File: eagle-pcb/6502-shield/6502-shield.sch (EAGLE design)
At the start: 28 parts, among them CON1 M20-7821646-FEM-HDR, SW1 MCSLPT4644B1TR-TACT-SW, SW2 PCM12SMTR-SPDT-RIGHT-ANG, U1 AT28C256TSOP-28, U13 74HC32TSSOP-14, U17 74HC04TSSOP-14, U2 W65C02S, U3 AS6C62256, U4 W65C22, U5 MM74HC00TSSOP, U6 SE555QS, U7 SE555QS, U8 SE555QS

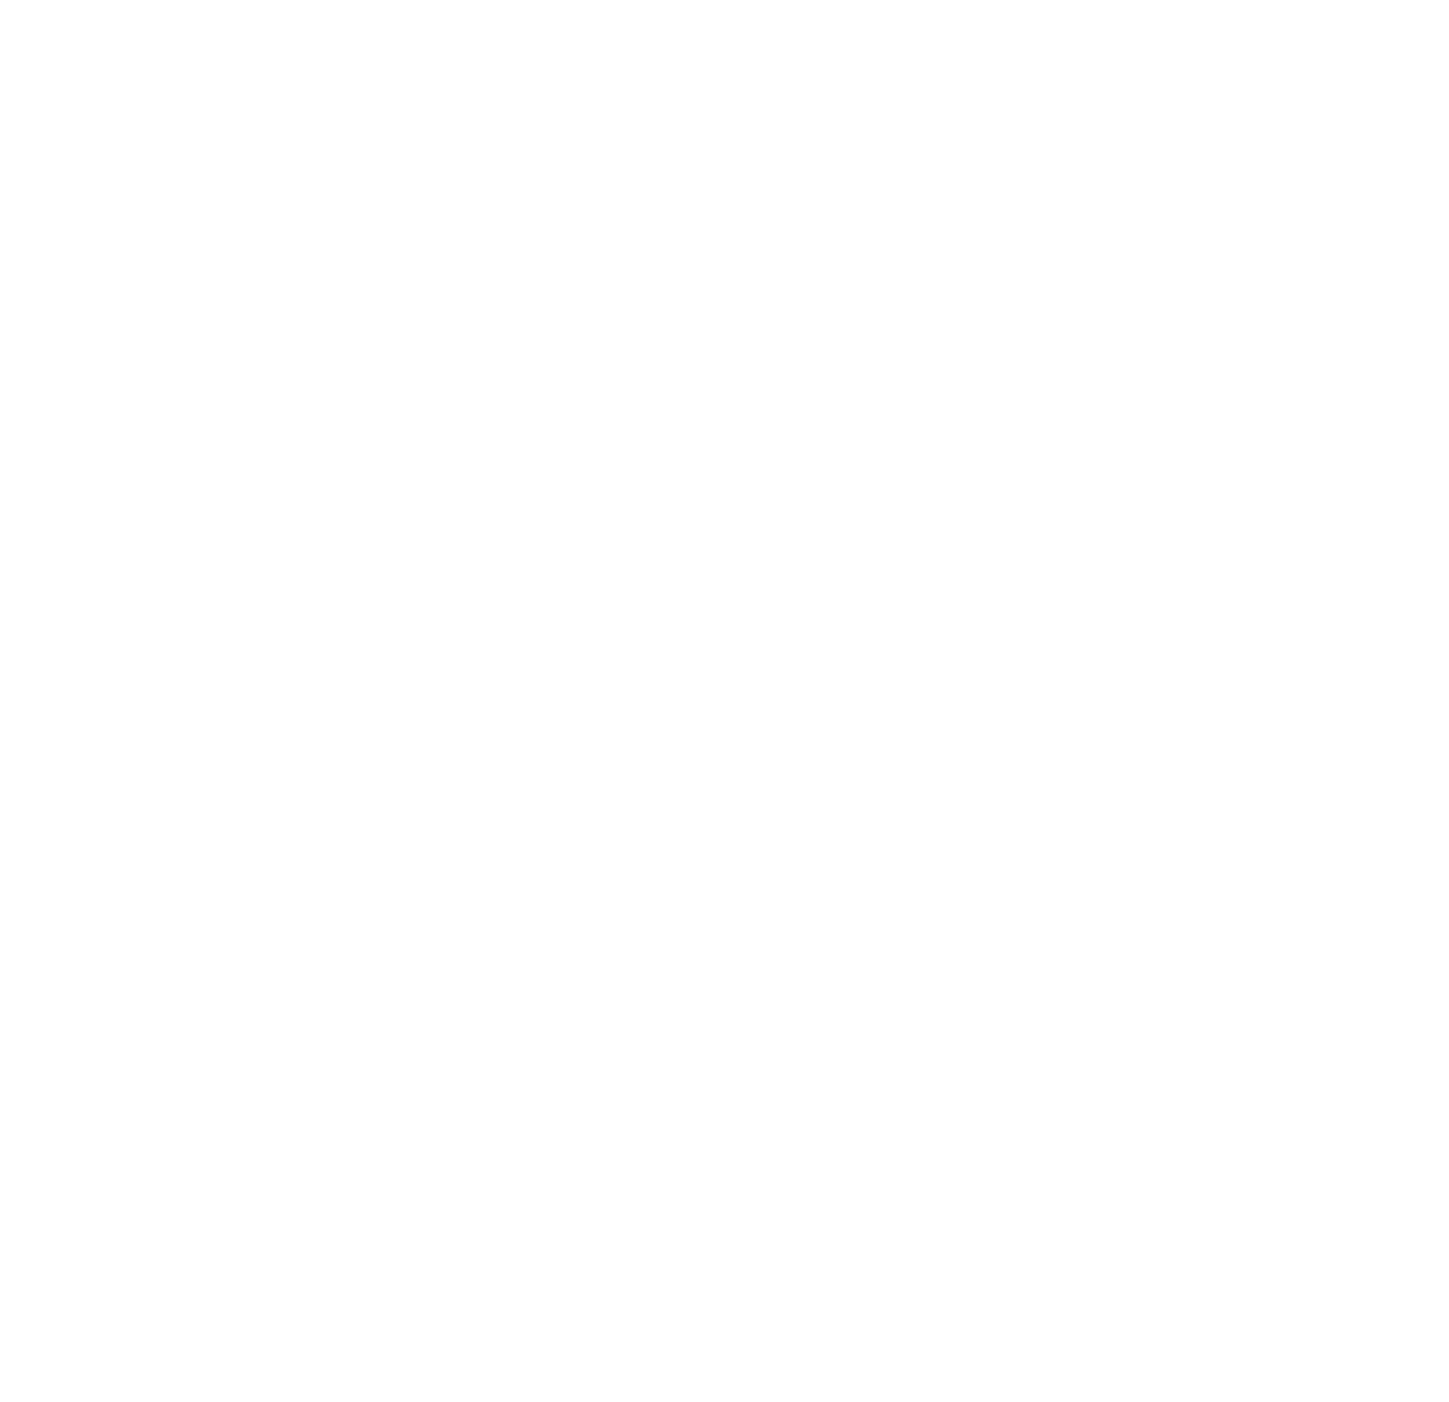
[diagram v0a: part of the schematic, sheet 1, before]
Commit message: added lattice machx02-256 FPGA in tqfp100 package - symbol, footprint, 3d model
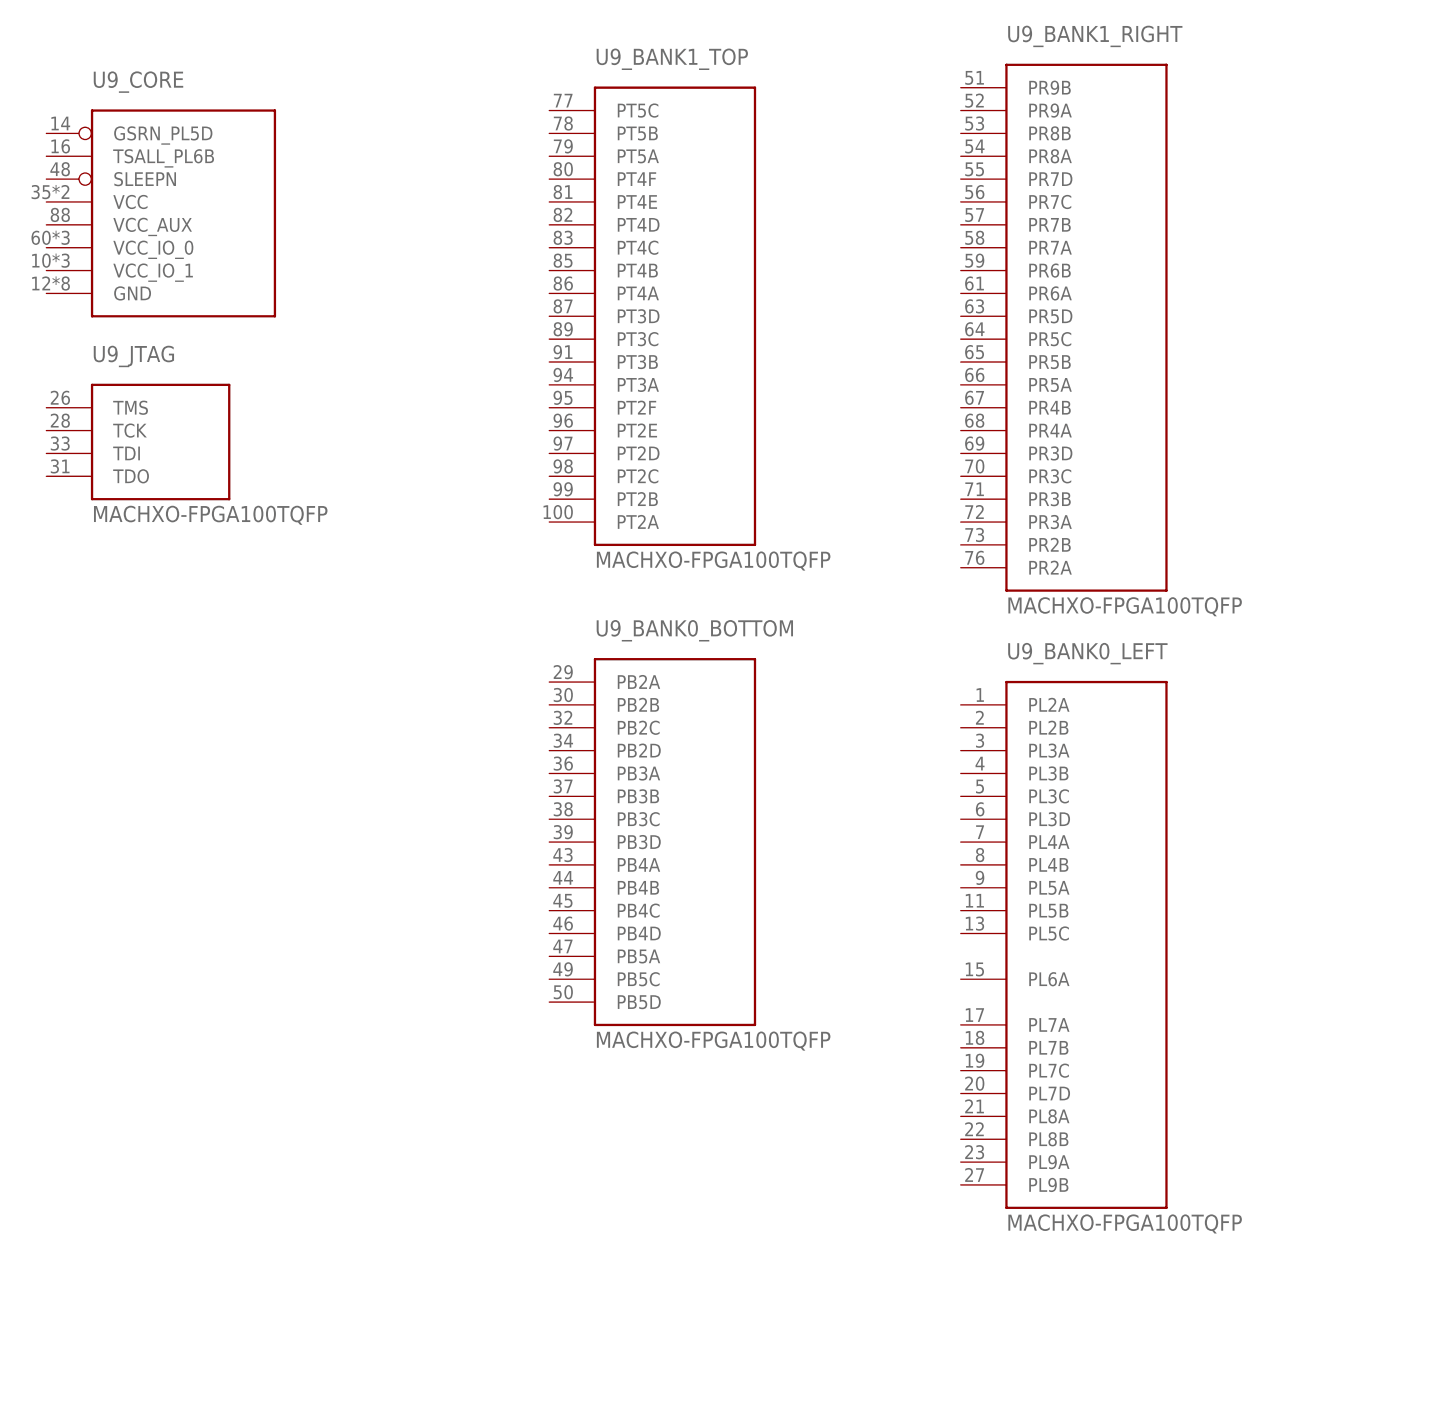
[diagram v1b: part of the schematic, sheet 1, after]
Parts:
- added U9: MACHXO-FPGA100TQFP, 6502-shield:MACHXO-FPGA100TQFP
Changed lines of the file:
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@@
 <setting verticaltext="up"/>
 </settings>
-<grid distance="0.01" unitdist="inch" unit="inch" style="lines" multiple="1" display="yes" altdistance="0.001" altunitdist="inch" altunit="inch"/>
+<grid distance="0.1" unitdist="inch" unit="inch" style="lines" multiple="1" display="no" altdistance="0.01" altunitdist="inch" altunit="inch"/>
 <layers>
 <layer number="1" name="Top" color="4" fill="1" visible="no" active="no"/>
@@
 <part name="GND22" library="supply1" library_urn="urn:adsk.eagle:library:371" deviceset="GND" device=""/>
 <part name="CON1" library="6502-shield" library_urn="urn:adsk.eagle:library:18477216" deviceset="M20-7821646-FEM-HDR" device="" package3d_urn="urn:adsk.eagle:package:18698632/1"/>
+<part name="U9" library="6502-shield" library_urn="urn:adsk.eagle:library:18477216" deviceset="MACHXO-FPGA" device="100TQFP" package3d_urn="urn:adsk.eagle:package:18828921/1"/>
 </parts>
 <sheets>
@@
 <attribute name="VALUE" x="195.58" y="37.846" size="1.27" layer="96"/>
 </instance>
+<instance part="U9" gate="_JTAG" x="-246.38" y="170.18" smashed="yes">
+<attribute name="NAME" x="-254" y="177.8" size="1.778" layer="95"/>
+<attribute name="VALUE" x="-254" y="160.02" size="1.778" layer="96"/>
+</instance>
+<instance part="U9" gate="_CORE" x="-243.84" y="195.58" smashed="yes">
+<attribute name="NAME" x="-254" y="208.28" size="1.778" layer="95"/>
+</instance>
+<instance part="U9" gate="_BANK1_TOP" x="-187.96" y="182.88" smashed="yes">
+<attribute name="NAME" x="-198.12" y="210.82" size="1.778" layer="95"/>
+<attribute name="VALUE" x="-198.12" y="154.94" size="1.778" layer="96"/>
+</instance>
+<instance part="U9" gate="_BANK1_RIGHT" x="-142.24" y="182.88" smashed="yes">
+<attribute name="NAME" x="-152.4" y="213.36" size="1.778" layer="95"/>
+<attribute name="VALUE" x="-152.4" y="149.86" size="1.778" layer="96"/>
+</instance>
+<instance part="U9" gate="_BANK0_LEFT" x="-142.24" y="114.3" smashed="yes">
+<attribute name="NAME" x="-152.4" y="144.78" size="1.778" layer="95"/>
+<attribute name="VALUE" x="-152.4" y="81.28" size="1.778" layer="96"/>
+</instance>
+<instance part="U9" gate="_BANK0_BOTTOM" x="-187.96" y="124.46" smashed="yes">
+<attribute name="NAME" x="-198.12" y="147.32" size="1.778" layer="95"/>
+<attribute name="VALUE" x="-198.12" y="101.6" size="1.778" layer="96"/>
+</instance>
 </instances>

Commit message: got the fpga based design done (first pass).  Notional parts placement, no routing.
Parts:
- removed C1: 1uF, rcl:C-USC0805
- removed C2, C5, C7: 0.01uF, rcl:C-USC0402
- removed C6: 0.1uF, rcl:C-USC0402
- removed CON1: M20-7821646-FEM-HDR, 6502-shield:M20-7821646-FEM-HDR
- removed U13: 74HC32TSSOP-14, 6502-shield:74HC32TSSOP-14
- removed U17: 74HC04TSSOP-14, 6502-shield:74HC04TSSOP-14
- removed U6, U7, U8: SE555QS, 6502-shield:SE555QS
- removed U9: MACHXO-FPGA100TQFP, 6502-shield:MACHXO-FPGA100TQFP
- added D1, D2, D3, D4, D5, D6, D7: (no value), we-led:WL-SMCD_0603_150060SS55040
- added D10, D8, D9: ACDC02-41SGWA-DUAL-7SEG, 6502-shield:ACDC02-41SGWA-DUAL-7SEG
- added JP1: (no value), pinhead:PINHD-2X3
- added JP2: (no value), pinhead:PINHD-2X8
- added JP3: (no value), pinhead:PINHD-1X3
- added R10, R11, R12, R13, R14, R15, R16, R17: 330, rcl:R-US_R0402
- added R18: 10K, rcl:R-US_R0402
- added R19: 10K, 6502-shield:TRIMPOTTC33X
- added R8, R9: 390, rcl:R-US_R0402
- added SJ1: (no value), jumper:SJ2W
- added SW3: MCSLPT4644B1TR-TACT-SW, 6502-shield:MCSLPT4644B1TR-TACT-SW
- added U$1: CRYSTAL-OSC-DIP8/4, 6502-shield:CRYSTAL-OSC-DIP8/4
- R1: value 1K -> 10K; device rcl:R-US_R0603 -> rcl:R-US_R0402
- R2, R5, R7: value 1K -> 390; device rcl:R-US_R0603 -> rcl:R-US_R0402
- R3: value 1K -> 4.7K; device rcl:R-US_R0603 -> rcl:R-US_R0402
- R4: value 1M -> 390; device rcl:R-US_R0603 -> rcl:R-US_R0402
- R6: value 1M -> 390; device 6502-shield:TRIMPOTTC33X -> rcl:R-US_R0402
- U5: value MM74HC00TSSOP -> MACHXO-FPGA100TQFP; device 6502-shield:MM74HC00TSSOP -> 6502-shield:MACHXO-FPGA100TQFP
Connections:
- removed net CLK_0: U5G$1.A, U6.OUT
- removed net CLK_1: U5G$2.B, U7.OUT
- removed net CLK_HALT: U17G$2.A
- removed net CLK_SELECT: U17G$1.A, U5G$1.B, U8.OUT
- removed net TRIG: C1.1, R6.E, U6.THRES, U6.TRIG
- new net BE: U2.BE, U5_BANK0_BOTTOM.PB3C
- new net CLK_SEL: SJ1.2, U5_BANK0_LEFT.PL7B
- new net DIGIT1_EN: D8.1EN, U5_BANK1_TOP.PT3D
- new net DIGIT2_EN: D8.2EN, U5_BANK1_TOP.PT3C
- new net DIGIT3_EN: D9.1EN, U5_BANK1_TOP.PT3B
- new net DIGIT4_EN: D9.2EN, U5_BANK1_TOP.PT3A
- new net DIGIT5_EN: D10.1EN, U5_BANK1_TOP.PT2F
- new net DIGIT6_EN: D10.2EN, U5_BANK1_TOP.PT2E
- new net DIGIT_A: R10.2, U5_BANK1_TOP.PT5B
- new net DIGIT_B: R11.2, U5_BANK1_TOP.PT5A
- new net DIGIT_C: R12.2, U5_BANK1_TOP.PT4F
- new net DIGIT_D: R13.2, U5_BANK1_TOP.PT4E
- new net DIGIT_DP: R17.2, U5_BANK1_TOP.PT4A
- new net DIGIT_E: R14.2, U5_BANK1_TOP.PT4D
- new net DIGIT_F: R15.2, U5_BANK1_TOP.PT4C
- new net DIGIT_G: R16.2, U5_BANK1_TOP.PT4B
- new net DMA: PCB1.47, U5_BANK0_BOTTOM.PB2C
- new net IO_EN: U4.CS2B, U5_BANK0_BOTTOM.PB3A
- new net IRQN: U2.IRQB, U4.IRQB, U5_BANK0_BOTTOM.PB4B
- new net N$15: D4.C, R9.2
- new net N$16: D4.A, U5_BANK1_TOP.PT2A
- new net N$17: D7.A, U5_BANK1_TOP.PT2B
- new net N$18: D3.A, U5_BANK1_TOP.PT2C
- new net N$19: D6.A, U5_BANK1_TOP.PT2D
- new net N$20: D1.C, R4.1
- new net N$21: D2.C, R2.1
- new net N$22: D5.C, R5.1
- new net N$23: D10.1A, D10.2A, D8.1A, D8.2A, D9.1A, D9.2A, R10.1
- new net N$24: D10.1B, D10.2B, D8.1B, D8.2B, D9.1B, D9.2B, R11.1
- new net N$25: D10.1C, D10.2C, D8.1C, D8.2C, D9.1C, D9.2C, R12.1
- new net N$26: D10.1D, D10.2D, D8.1D, D8.2D, D9.1D, D9.2D, R13.1
- new net N$27: D10.1E, D10.2E, D8.1E, D8.2E, D9.1E, D9.2E, R14.1
- new net N$28: D10.1F, D10.2F, D8.1F, D8.2F, D9.1F, D9.2F, R15.1
- new net N$29: D10.1G, D10.2G, D8.1G, D8.2G, D9.1G, D9.2G, R16.1
- new net N$30: D10.1DP, D10.2DP, D8.1DP, D8.2DP, D9.1DP, D9.2DP, R17.1
- new net N$31: R18.1, U2.RDY
- new net N$32: JP3.2, R19.S
- new net N$34: U$1.OUT, U5_BANK0_LEFT.PL7A
- new net OE: PCB1.39, U1.OE, U3.OE, U5_BANK1_RIGHT.PR2B
- new net RAM_EN: U3.CE, U5_BANK1_RIGHT.PR2A
- new net RESETN: U2.RESB, U4.RESB, U5_BANK0_BOTTOM.PB3D
- new net ROM_EN: U1.CE, U5_BANK1_TOP.PT5C
- new net ROM_PGM: PCB1.45, U5_BANK0_BOTTOM.PB2D
- new net RW: U2.RWB, U4.R/WB, U5_BANK0_BOTTOM.PB4A
- new net WE: PCB1.41, U1.WE, U3.WE, U5_BANK1_RIGHT.PR3A
- net A0: now also PCB1.22, U5_BANK1_RIGHT.PR8A
- net A1: now also PCB1.24, U5_BANK1_RIGHT.PR7D
- net A10: now also PCB1.42, U5_BANK1_RIGHT.PR5A
- net A11: now also PCB1.44, U5_BANK1_RIGHT.PR4B
- net A12: now also PCB1.46, U5_BANK1_RIGHT.PR4A
- net A13: now also PCB1.48, U5_BANK1_RIGHT.PR3D
- net A14: now also PCB1.50, U5_BANK1_RIGHT.PR3C
- net A15: now also PCB1.52, U5_BANK1_RIGHT.PR3B
- net A2: now also PCB1.26, U5_BANK1_RIGHT.PR7C
- net A3: now also PCB1.28, U5_BANK1_RIGHT.PR7B
- net A4: now also PCB1.30, U5_BANK1_RIGHT.PR7A
- net A5: now also PCB1.32, U5_BANK1_RIGHT.PR6B
- net A6: now also PCB1.34, U5_BANK1_RIGHT.PR6A
- net A7: now also PCB1.36, U5_BANK1_RIGHT.PR5D
- net A8: now also PCB1.38, U5_BANK1_RIGHT.PR5C
- net A9: now also PCB1.40, U5_BANK1_RIGHT.PR5B
- net CLK: now also PCB1.43, U2.PHI2, U5_BANK0_BOTTOM.PB3B; no longer U5G$3.Y
- net D0: now also PCB1.23, U5_BANK0_BOTTOM.PB4C
- net D1: now also PCB1.25, U5_BANK0_BOTTOM.PB4D
- net D2: now also PCB1.27, U5_BANK0_BOTTOM.PB5A
- net D3: now also PCB1.29, U5_BANK0_BOTTOM.PB5C
- net D4: now also PCB1.31, U5_BANK0_BOTTOM.PB5D
- net D5: now also PCB1.33, U5_BANK1_RIGHT.PR9B
- net D6: now also PCB1.35, U5_BANK1_RIGHT.PR9A
- net D7: now also PCB1.37, U5_BANK1_RIGHT.PR8B
- net GND: now also JP1.5, JP3.3, R19.A, R2.2, R3.1, R4.2, R5.2, R6.1, R7.1, R8.1, R9.1, SJ1.3, SW2.3, SW3.T2, U$1.GND, U5_CORE.GND; no longer C1.2, C2.2, C5.2, C6.2, C7.2, SW2.1, U13G$5.GND, U17G$7.GND, U2.VSS@1, U2.VSS@2, U2.VSS@3, U5G$5.GND, U6.GND, U7.GND, U8.GND, U8.THRES
- net N$1: now also R1.1, U5_CORE.SLEEPN; no longer R2.2, R6.S
- net N$10: now also D2.A, U5_BANK0_LEFT.PL2B; no longer U17G$1.Y, U5G$2.A
- net N$11: now also D5.A, U5_BANK0_LEFT.PL3A; no longer U13G$1.A, U5G$1.Y
- net N$12: now also D6.C, R6.2; no longer U13G$1.B, U5G$2.Y
- net N$13: now also D3.C, R7.2; no longer U13G$1.Y, U5G$3.A
- net N$14: now also D7.C, R8.2; no longer U17G$2.Y, U5G$3.B
- net N$2: now also SW3.T4, U5_BANK0_LEFT.PL3C; no longer C2.1, U6.CONT
- net N$3: now also SW1.T4, U5_CORE.GSRN_PL5D; no longer R1.1, R2.1, U6.DISCH
- net N$4: now also JP1.2, U5_JTAG.TDO; no longer R3.1, SW1.T3, U7.TRIG
- net N$5: now also JP1.3, U5_JTAG.TMS; no longer C5.1, U7.CONT
- net N$6: now also JP1.4, U5_JTAG.TDI; no longer C6.1, R4.1, U7.DISCH, U7.THRES
- net N$7: now also JP1.6, R3.2, U5_JTAG.TCK; no longer R5.1, SW2.2, U8.TRIG
- net N$8: now also SW2.1, U5_BANK0_LEFT.PL3B; no longer R7.1, SW2.3, U8.RESET
- net N$9: now also D1.A, U5_BANK0_LEFT.PL2A; no longer C7.1, U8.CONT
- net PA0: now also JP2.1
- net PA1: now also JP2.3
- net PA2: now also JP2.5
- net PA3: now also JP2.7
- net PA4: now also JP2.9
- net PA5: now also JP2.11; no longer CON1.4
- net PA6: now also JP2.13; no longer CON1.5
- net PA7: now also JP2.15; no longer CON1.6
- net PB0: now also JP2.2; no longer CON1.7
- net PB1: now also JP2.4; no longer CON1.8
- net PB2: now also JP2.6; no longer CON1.9
- net PB3: now also JP2.8; no longer CON1.10
- net PB4: now also JP2.10; no longer CON1.11
- net PB5: now also JP2.12; no longer CON1.12
- net PB6: now also JP2.14; no longer CON1.13
- net PB7: now also JP2.16; no longer CON1.14
- net VCC: now also JP1.1, JP3.1, PCB1.3.3V, R18.2, U$1.VCC, U2.NMIB, U2.VDD, U4.CS1, U5_CORE.VCC, U5_CORE.VCC_AUX, U5_CORE.VCC_IO_0, U5_CORE.VCC_IO_1; no longer PCB1.+5V., PCB1.+5V.., PCB1.5V, R3.2, R4.2, R5.2, R7.2, U13G$5.VCC, U17G$7.VCC, U2.VDD@1, U2.VDD@2, U5G$5.VCC, U6.RESET, U6.VCC, U7.RESET, U7.VCC, U8.VCC
